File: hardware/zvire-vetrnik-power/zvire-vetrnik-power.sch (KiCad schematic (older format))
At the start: 45 parts, among them J1 12V IN, J2 ~SHORT, J3 UART, J4 ENABLE, J5 RELAYS, M1 12V / 0,9A max, Q1 BCP56-16, Q2 BC847, Q3 BC846, Q4 BC846, Q5 BC846, Q6 BC846, Q7 BC846, U1 LTV-847, U2 H11L1, U3 H11L1, U4 LTV-847

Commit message: Pred off-board soucastkami
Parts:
- added H1, H2, H3, H4: MountingHole, MountingHole:MountingHole_3.2mm_M3, symbol Mechanical:MountingHole
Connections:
- net 3V3_UART: now also J3.1 (Pin_1); no longer J3.4 (Pin_4)
- net GND: now also J3.4 (Pin_4); no longer J3.1 (Pin_1)
- net RX: now also J3.3 (Pin_3); no longer J3.2 (Pin_2)
- net TX: now also J3.2 (Pin_2); no longer J3.3 (Pin_3)
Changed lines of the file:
@@
 L Connector_Generic:Conn_01x04 J3
 U 1 1 630F8C0A
-P 5300 2800
-F 0 "J3" H 5500 2700 50  0000 C CNN
-F 1 "UART" H 5450 2800 50  0000 C CNN
-F 2 "Connector_Molex:Molex_KK-254_AE-6410-04A_1x04_P2.54mm_Vertical" H 5300 2800 50  0001 C CNN
-F 3 "~" H 5300 2800 50  0001 C CNN
-	1    5300 2800
-	-1   0    0    1
+P 5300 2700
+F 0 "J3" H 5500 2600 50  0000 C CNN
+F 1 "UART" H 5450 2700 50  0000 C CNN
+F 2 "Connector_Molex:Molex_KK-254_AE-6410-04A_1x04_P2.54mm_Vertical" H 5300 2700 50  0001 C CNN
+F 3 "~" H 5300 2700 50  0001 C CNN
+	1    5300 2700
+	-1   0    0    -1
 $EndComp
 $Comp
@@
 	3700 5900 3600 5900
 Connection ~ 3600 5900
+$Comp
+L Mechanical:MountingHole H1
+U 1 1 630F4A2F
+P 750 700
+F 0 "H1" H 850 746 50  0000 L CNN
+F 1 "MountingHole" H 850 655 50  0000 L CNN
+F 2 "MountingHole:MountingHole_3.2mm_M3" H 750 700 50  0001 C CNN
+F 3 "~" H 750 700 50  0001 C CNN
+	1    750  700
+	1    0    0    -1
+$EndComp
+$Comp
+L Mechanical:MountingHole H3
+U 1 1 630F8913
+P 1500 700
+F 0 "H3" H 1600 746 50  0000 L CNN
+F 1 "MountingHole" H 1600 655 50  0000 L CNN
+F 2 "MountingHole:MountingHole_3.2mm_M3" H 1500 700 50  0001 C CNN
+F 3 "~" H 1500 700 50  0001 C CNN
+	1    1500 700
+	1    0    0    -1
+$EndComp
+$Comp
+L Mechanical:MountingHole H2
+U 1 1 630F8C70
+P 750 900
+F 0 "H2" H 850 946 50  0000 L CNN
+F 1 "MountingHole" H 850 855 50  0000 L CNN
+F 2 "MountingHole:MountingHole_3.2mm_M3" H 750 900 50  0001 C CNN
+F 3 "~" H 750 900 50  0001 C CNN
+	1    750  900
+	1    0    0    -1
+$EndComp
+$Comp
+L Mechanical:MountingHole H4
+U 1 1 630F8ECB
+P 1500 900
+F 0 "H4" H 1600 946 50  0000 L CNN
+F 1 "MountingHole" H 1600 855 50  0000 L CNN
+F 2 "MountingHole:MountingHole_3.2mm_M3" H 1500 900 50  0001 C CNN
+F 3 "~" H 1500 900 50  0001 C CNN
+	1    1500 900
+	1    0    0    -1
+$EndComp
 $EndSCHEMATC

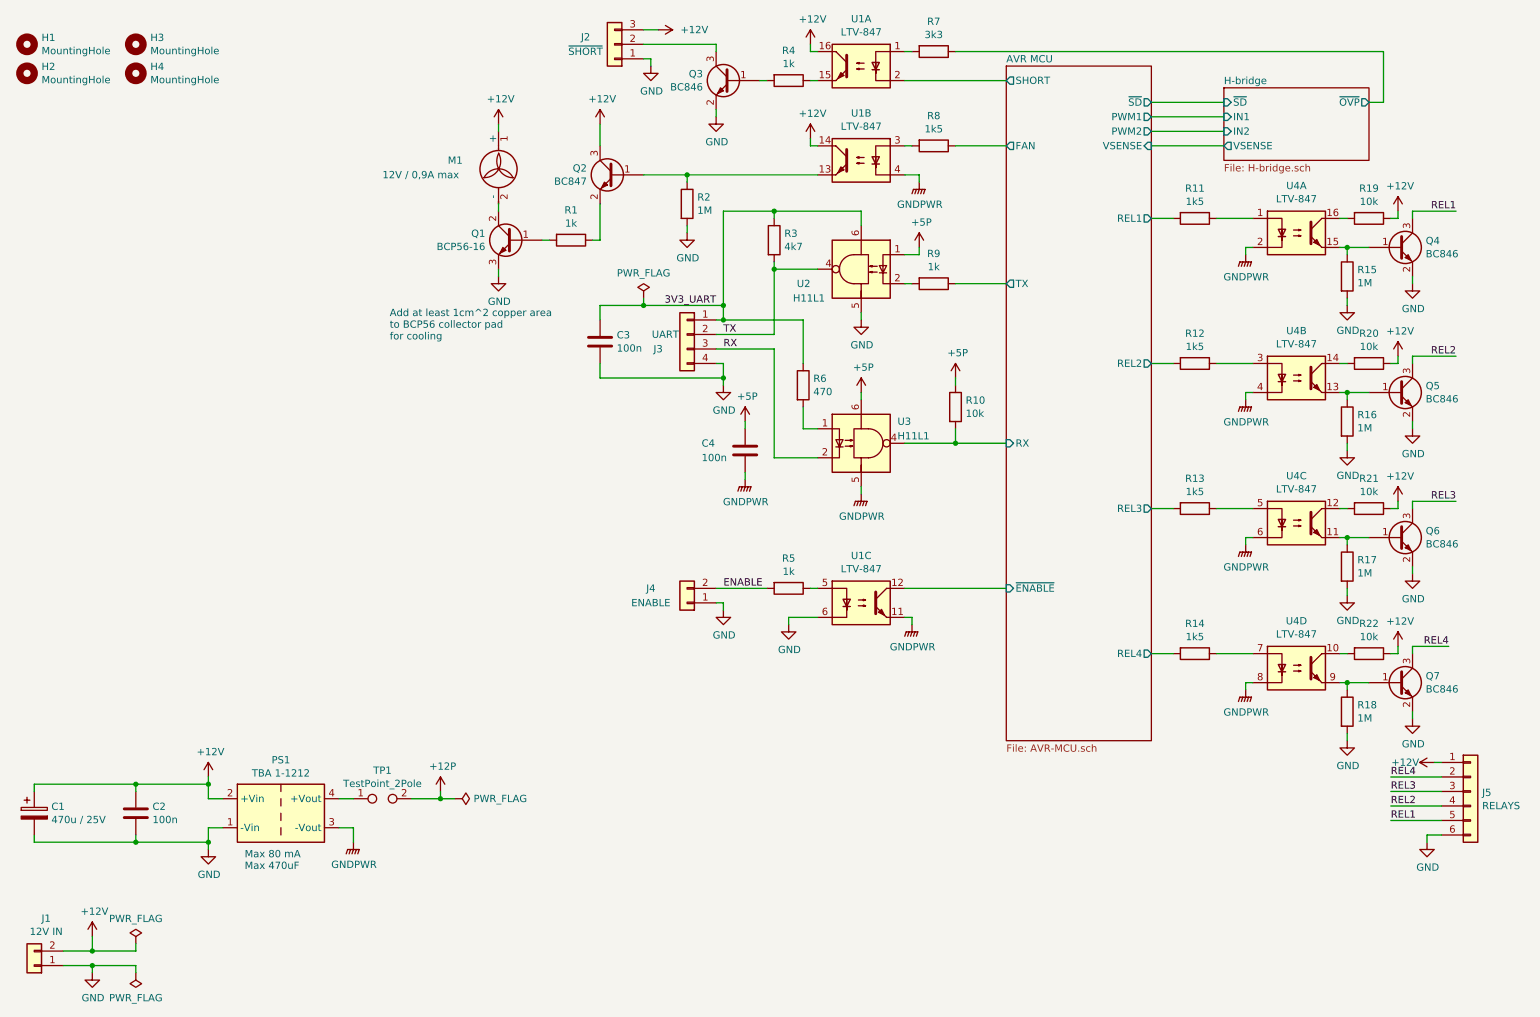
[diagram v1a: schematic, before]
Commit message: Vyrobena verze power PCB
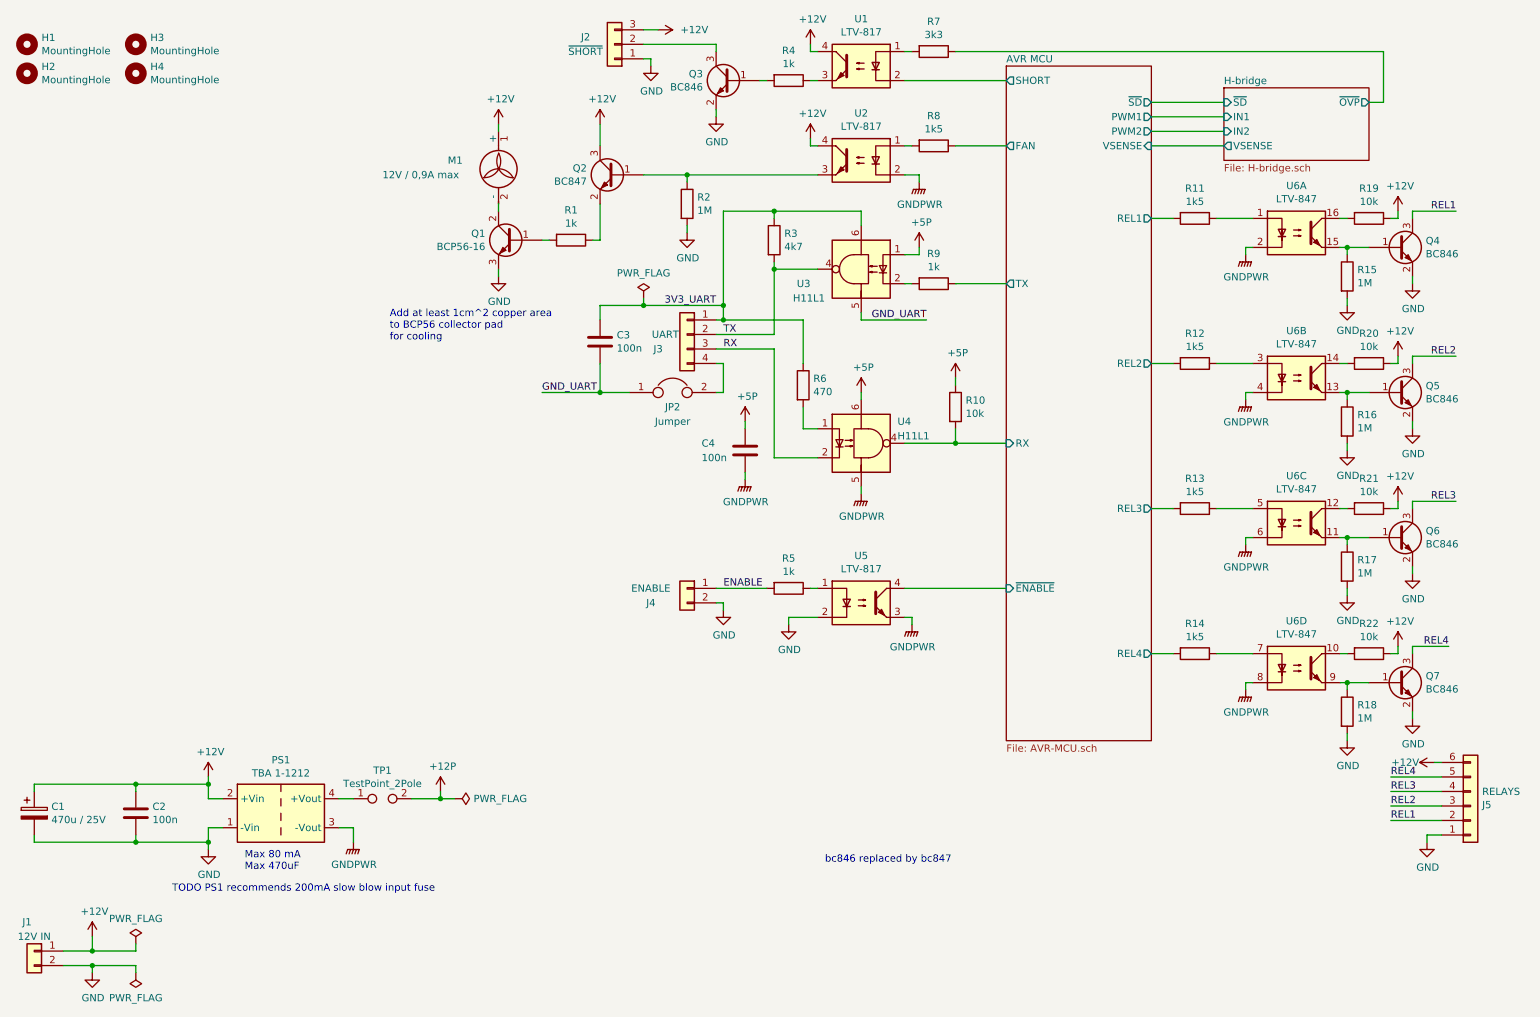
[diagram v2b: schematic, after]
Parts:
- removed U1: LTV-847, Package_DIP:DIP-16_W7.62mm, symbol Isolator:LTV-847
- added JP2: Jumper, Resistor_SMD:R_1206_3216Metric_Pad1.30x1.75mm_HandSolder, symbol Device:Jumper
- added U1, U2, U5: LTV-817, Package_DIP:DIP-4_W7.62mm, symbol Isolator:LTV-817
- renumbered U2 to U3, U3 to U4, U4 to U6
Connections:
- net +12V: now also J1.1 (Pin_1), J5.6 (Pin_6), U1.4, U2.4; no longer J1.2 (Pin_2), J5.1 (Pin_1)
- net AVR MCU/SHORT: now also U1.2
- net AVR MCU/~ENABLE: now also U5.4
- net ENABLE: now also J4.1 (Pin_1); no longer J4.2 (Pin_2)
- net GND: now also J1.2 (Pin_2), J4.2 (Pin_2), J5.1 (Pin_1), U5.2; no longer C3.2, J1.1 (Pin_1), J3.4 (Pin_4), J4.1 (Pin_1), J5.6 (Pin_6), U3.5
- net GNDPWR: now also U2.2, U5.3
- net REL1: now also J5.2 (Pin_2); no longer J5.5 (Pin_5)
- net REL2: now also J5.3 (Pin_3); no longer J5.4 (Pin_4)
- net REL3: now also J5.4 (Pin_4); no longer J5.3 (Pin_3)
- net REL4: now also J5.5 (Pin_5); no longer J5.2 (Pin_2)
- net at R7.2: now also U1.1
- net at R4.1: now also U1.3
- net at R5.1: now also U5.1
- net at Q2.1 (B), R2.1: now also U2.3
- net at R8.2: now also U2.1
- new net: J3.4 (Pin_4), JP2.2
- new net GND_UART: C3.2, JP2.1, U3.5
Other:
- note added: "TODO PS1 recommends 200mA slow blow input fuse"
- note added: "bc846 replaced by bc847"

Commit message: Add note to schematic
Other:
- note added: "TODO 4-pin PC fan connector"
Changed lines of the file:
@@
 Text Notes 1750 6550 0    50   ~ 0
 TODO PS1 recommends 200mA slow blow input fuse
+Text Notes 2450 1800 0    50   ~ 0
+TODO 4-pin PC fan connector
 $EndSCHEMATC

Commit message: [power] [HW] Fix connector label for SHORT
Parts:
- J2: value ~SHORT -> SHORT
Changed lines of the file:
@@
 P 4800 700
 F 0 "J2" H 5000 650 50  0000 C CNN
-F 1 "~SHORT" H 5000 750 50  0000 C CNN
+F 1 "SHORT" H 5000 750 50  0000 C CNN
 F 2 "Connector_Molex:Molex_KK-254_AE-6410-03A_1x03_P2.54mm_Vertical" H 4800 700 50  0001 C CNN
 F 3 "~" H 4800 700 50  0001 C CNN
